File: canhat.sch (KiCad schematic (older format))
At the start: 24 parts, among them J1 Raspberry_Pi_2_3, J2 CAN In, J3 CAN Out, U1 MCP2515-xSO, U2 SN65HVD234, U3 AT24C32-SSHM, Y1 16MHz

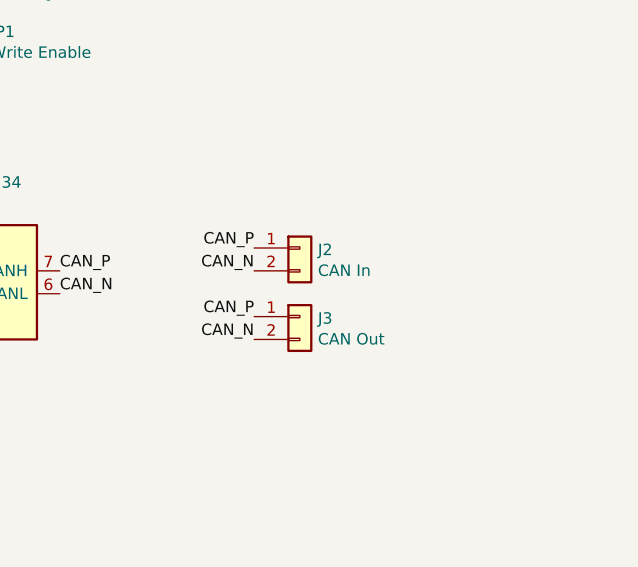
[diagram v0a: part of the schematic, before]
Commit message: Replaced CAN terminals with single block
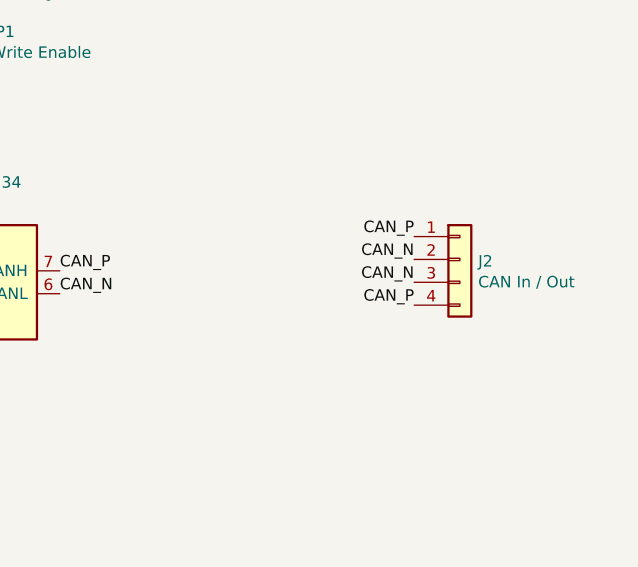
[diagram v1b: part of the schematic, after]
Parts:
- removed J2: CAN In, TerminalBlock_TE-Connectivity:TerminalBlock_TE_282834-2_1x02_P2.54mm_Horizontal, symbol Connector_Generic:Conn_01x02
- removed J3: CAN Out, TerminalBlock_TE-Connectivity:TerminalBlock_TE_282834-2_1x02_P2.54mm_Horizontal, symbol Connector_Generic:Conn_01x02
- added J2: CAN In / Out, TerminalBlock_TE-Connectivity:TerminalBlock_TE_282834-4_1x04_P2.54mm_Horizontal, symbol Connector_Generic:Conn_01x04
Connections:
- net CAN_N: now also J2.2 (Pin_2), J2.3 (Pin_3)
- net CAN_P: now also J2.1 (Pin_1), J2.4 (Pin_4)
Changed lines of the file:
@@
 Sheet 1 1
 Title "CAN HAT for Raspberry Pi"
-Date "2019-04-05"
-Rev "1"
+Date "2019-04-29"
+Rev "2"
 Comp "© 2019 Gregor Riepl"
 Comment1 ""
@@
 $EndComp
 $Comp
-L Connector_Generic:Conn_01x02 J2
-U 1 1 5CA2AC48
-P 9450 3200
-F 0 "J2" H 9529 3192 50  0000 L CNN
-F 1 "CAN In" H 9529 3101 50  0000 L CNN
-F 2 "TerminalBlock_TE-Connectivity:TerminalBlock_TE_282834-2_1x02_P2.54mm_Horizontal" H 9450 3200 50  0001 C CNN
-F 3 "~" H 9450 3200 50  0001 C CNN
-	1    9450 3200
-	1    0    0    -1
-$EndComp
-$Comp
-L Connector_Generic:Conn_01x02 J3
-U 1 1 5CA2B324
-P 9450 3500
-F 0 "J3" H 9529 3492 50  0000 L CNN
-F 1 "CAN Out" H 9529 3401 50  0000 L CNN
-F 2 "TerminalBlock_TE-Connectivity:TerminalBlock_TE_282834-2_1x02_P2.54mm_Horizontal" H 9450 3500 50  0001 C CNN
-F 3 "~" H 9450 3500 50  0001 C CNN
-	1    9450 3500
-	1    0    0    -1
-$EndComp
-$Comp
 L Mechanical:MountingHole H1
 U 1 1 5CA2E828
@@
 Text Label 8400 3400 0    50   ~ 0
 CAN_N
-Text Label 9250 3200 2    50   ~ 0
+Text Label 9950 3150 2    50   ~ 0
 CAN_P
-Text Label 9250 3500 2    50   ~ 0
+Text Label 9950 3450 2    50   ~ 0
 CAN_P
-Text Label 9250 3300 2    50   ~ 0
+Text Label 9950 3250 2    50   ~ 0
 CAN_N
-Text Label 9250 3600 2    50   ~ 0
+Text Label 9950 3350 2    50   ~ 0
 CAN_N
 $Comp
@@
 	1    0    0    -1
 $EndComp
+$Comp
+L Connector_Generic:Conn_01x04 J2
+U 1 1 5CC6B3E9
+P 10150 3250
+F 0 "J2" H 10230 3242 50  0000 L CNN
+F 1 "CAN In / Out" H 10230 3151 50  0000 L CNN
+F 2 "TerminalBlock_TE-Connectivity:TerminalBlock_TE_282834-4_1x04_P2.54mm_Horizontal" H 10150 3250 50  0001 C CNN
+F 3 "~" H 10150 3250 50  0001 C CNN
+	1    10150 3250
+	1    0    0    -1
+$EndComp

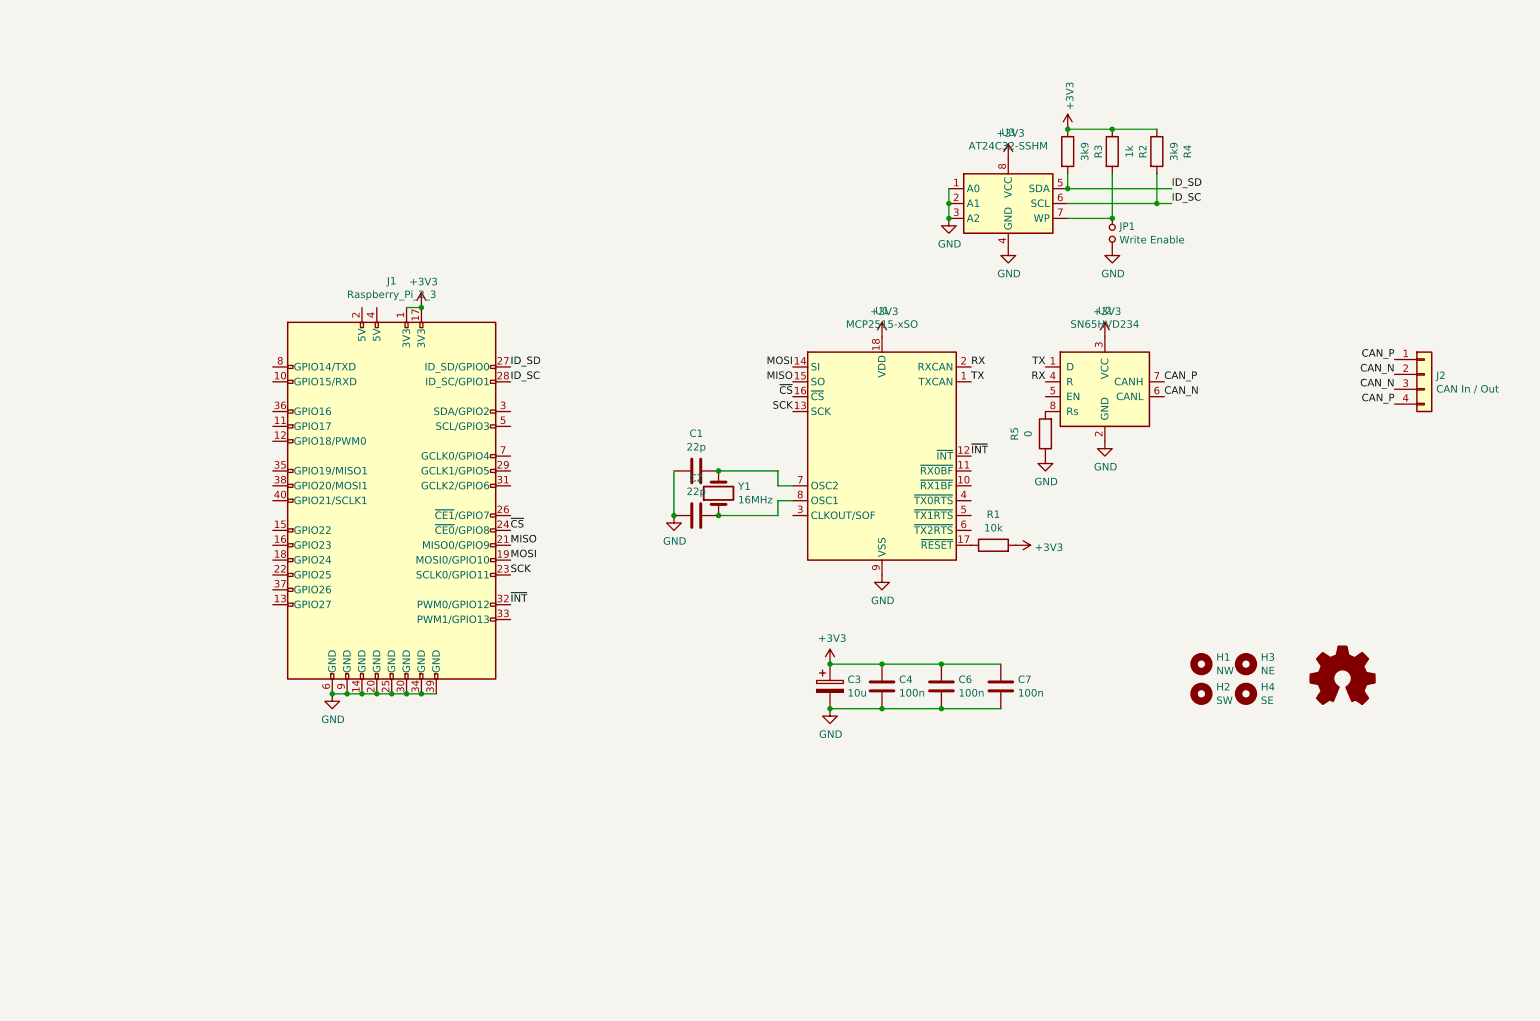
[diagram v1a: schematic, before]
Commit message: Added 5V power terminal
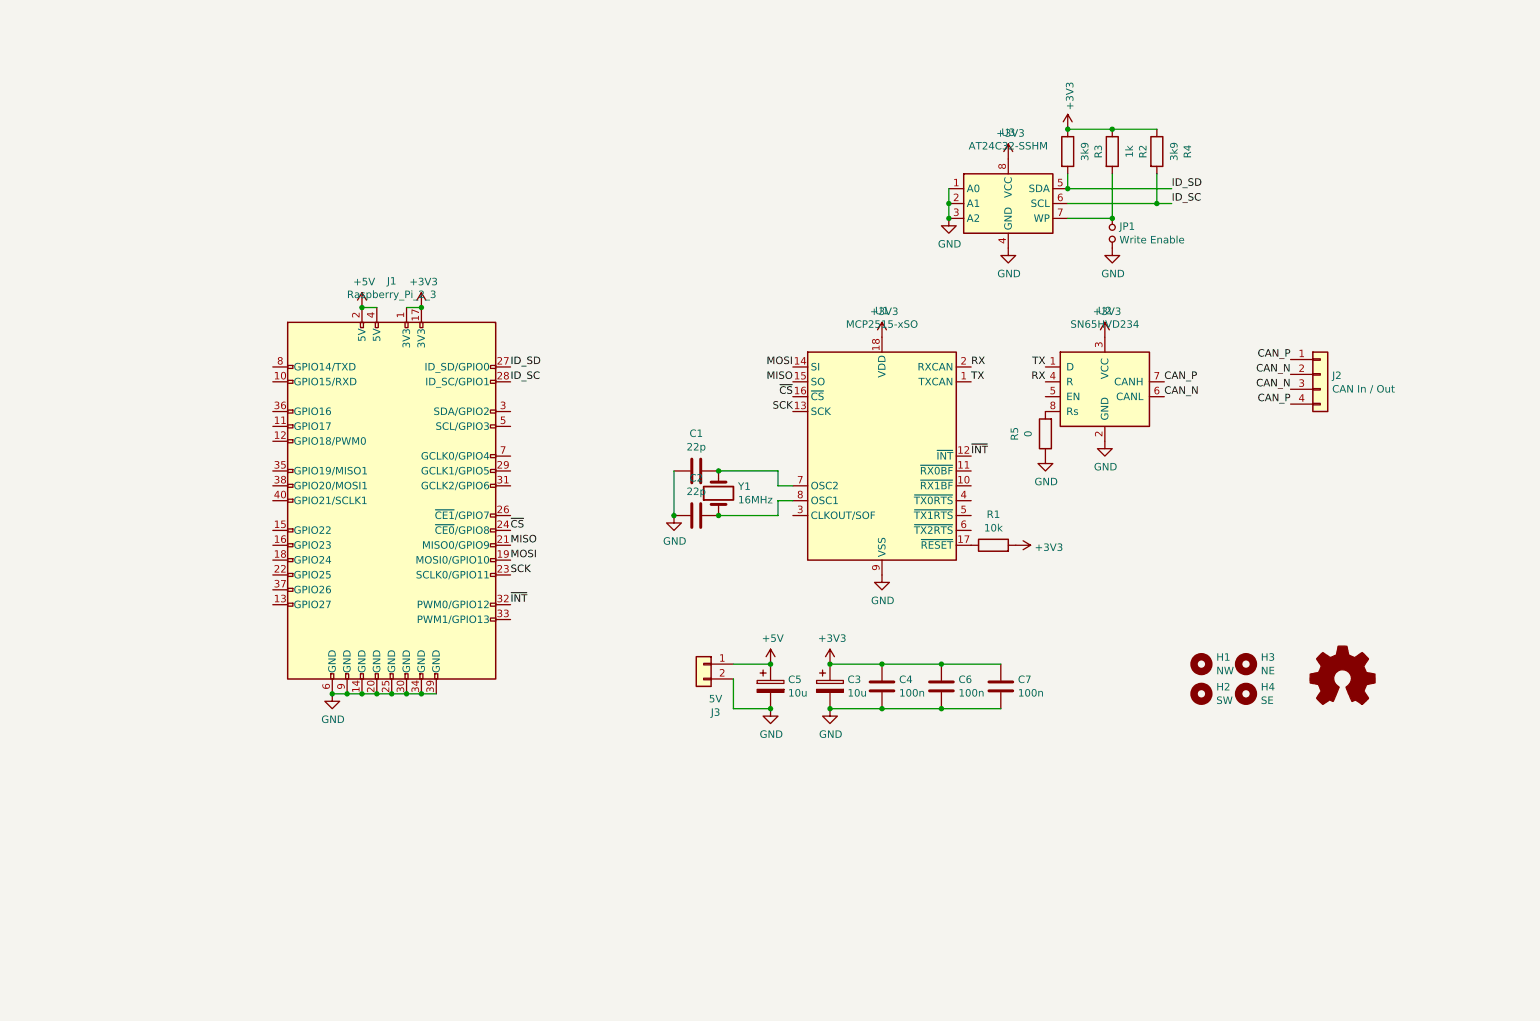
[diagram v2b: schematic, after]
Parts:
- added C5: 10u, Capacitor_Tantalum_SMD:CP_EIA-7343-31_Kemet-D_Pad2.25x2.55mm_HandSolder, symbol Device:CP
- added J3: 5V, TerminalBlock_TE-Connectivity:TerminalBlock_TE_282834-2_1x02_P2.54mm_Horizontal, symbol Connector_Generic:Conn_01x02
- C3: footprint Capacitor_THT:CP_Radial_D5.0mm_P2.00mm -> Capacitor_Tantalum_SMD:CP_EIA-7343-31_Kemet-D_Pad2.25x2.55mm_HandSolder
- Y1: footprint Crystal:Crystal_SMD_HC49-SD_HandSoldering -> Crystal:Crystal_SMD_HC49-SD
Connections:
- net GND: now also C5.2, J3.2 (Pin_2)
- net +5V: now reaches J1.2 (5V)
- net +5V: now also J1.4 (5V), C5.1, J3.1 (Pin_1)
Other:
- moved on the sheet: J2
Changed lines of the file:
@@
 Sheet 1 1
 Title "CAN HAT for Raspberry Pi"
-Date "2019-04-29"
+Date "2019-05-01"
 Rev "2"
 Comp "© 2019 Gregor Riepl"
@@
 F 0 "Y1" V 5446 3919 50  0000 R CNN
 F 1 "16MHz" V 5355 3919 50  0000 R CNN
-F 2 "Crystal:Crystal_SMD_HC49-SD_HandSoldering" H 5400 4050 50  0001 C CNN
+F 2 "Crystal:Crystal_SMD_HC49-SD" H 5400 4050 50  0001 C CNN
 F 3 "~" H 5400 4050 50  0001 C CNN
 	1    5400 4050
@@
 F 0 "C3" H 6268 5396 50  0000 L CNN
 F 1 "10u" H 6268 5305 50  0000 L CNN
-F 2 "Capacitor_THT:CP_Radial_D5.0mm_P2.00mm" H 6188 5200 50  0001 C CNN
+F 2 "Capacitor_Tantalum_SMD:CP_EIA-7343-31_Kemet-D_Pad2.25x2.55mm_HandSolder" H 6188 5200 50  0001 C CNN
 F 3 "~" H 6150 5350 50  0001 C CNN
 	1    6150 5350
@@
 Text Label 8400 3400 0    50   ~ 0
 CAN_N
-Text Label 9950 3150 2    50   ~ 0
+Text Label 9250 3150 2    50   ~ 0
 CAN_P
-Text Label 9950 3450 2    50   ~ 0
+Text Label 9250 3450 2    50   ~ 0
 CAN_P
-Text Label 9950 3250 2    50   ~ 0
+Text Label 9250 3250 2    50   ~ 0
 CAN_N
-Text Label 9950 3350 2    50   ~ 0
+Text Label 9250 3350 2    50   ~ 0
 CAN_N
 $Comp
@@
 L Connector_Generic:Conn_01x04 J2
 U 1 1 5CC6B3E9
-P 10150 3250
-F 0 "J2" H 10230 3242 50  0000 L CNN
-F 1 "CAN In / Out" H 10230 3151 50  0000 L CNN
-F 2 "TerminalBlock_TE-Connectivity:TerminalBlock_TE_282834-4_1x04_P2.54mm_Horizontal" H 10150 3250 50  0001 C CNN
-F 3 "~" H 10150 3250 50  0001 C CNN
-	1    10150 3250
-	1    0    0    -1
-$EndComp
+P 9450 3250
+F 0 "J2" H 9530 3242 50  0000 L CNN
+F 1 "CAN In / Out" H 9530 3151 50  0000 L CNN
+F 2 "TerminalBlock_TE-Connectivity:TerminalBlock_TE_282834-4_1x04_P2.54mm_Horizontal" H 9450 3250 50  0001 C CNN
+F 3 "~" H 9450 3250 50  0001 C CNN
+	1    9450 3250
+	1    0    0    -1
+$EndComp
+$Comp
+L Connector_Generic:Conn_01x02 J3
+U 1 1 5CC8D2CE
+P 5300 5200
+F 0 "J3" H 5220 4875 50  0000 C CNN
+F 1 "5V" H 5220 4966 50  0000 C CNN
+F 2 "TerminalBlock_TE-Connectivity:TerminalBlock_TE_282834-2_1x02_P2.54mm_Horizontal" H 5300 5200 50  0001 C CNN
+F 3 "~" H 5300 5200 50  0001 C CNN
+	1    5300 5200
+	-1   0    0    -1
+$EndComp
+$Comp
+L power:+5V #PWR0111
+U 1 1 5CC8D443
+P 3000 2800
+F 0 "#PWR0111" H 3000 2650 50  0001 C CNN
+F 1 "+5V" H 3015 2973 50  0000 C CNN
+F 2 "" H 3000 2800 50  0001 C CNN
+F 3 "" H 3000 2800 50  0001 C CNN
+	1    3000 2800
+	1    0    0    -1
+$EndComp
+Wire Wire Line
+	3100 2800 3000 2800
+Connection ~ 3000 2800
+$Comp
+L power:+5V #PWR0112
+U 1 1 5CC8D96C
+P 5750 5200
+F 0 "#PWR0112" H 5750 5050 50  0001 C CNN
+F 1 "+5V" H 5765 5373 50  0000 C CNN
+F 2 "" H 5750 5200 50  0001 C CNN
+F 3 "" H 5750 5200 50  0001 C CNN
+	1    5750 5200
+	1    0    0    -1
+$EndComp
+$Comp
+L Device:CP C5
+U 1 1 5CC8DA64
+P 5750 5350
+F 0 "C5" H 5868 5396 50  0000 L CNN
+F 1 "10u" H 5868 5305 50  0000 L CNN
+F 2 "Capacitor_Tantalum_SMD:CP_EIA-7343-31_Kemet-D_Pad2.25x2.55mm_HandSolder" H 5788 5200 50  0001 C CNN
+F 3 "~" H 5750 5350 50  0001 C CNN
+	1    5750 5350
+	1    0    0    -1
+$EndComp
+$Comp
+L power:GND #PWR0114
+U 1 1 5CC8DAAA
+P 5750 5500
+F 0 "#PWR0114" H 5750 5250 50  0001 C CNN
+F 1 "GND" H 5755 5327 50  0000 C CNN
+F 2 "" H 5750 5500 50  0001 C CNN
+F 3 "" H 5750 5500 50  0001 C CNN
+	1    5750 5500
+	1    0    0    -1
+$EndComp
+Wire Wire Line
+	5500 5200 5750 5200
+Connection ~ 5750 5200
+Wire Wire Line
+	5500 5500 5750 5500
+Connection ~ 5750 5500
+Wire Wire Line
+	5500 5300 5500 5500
 $EndSCHEMATC

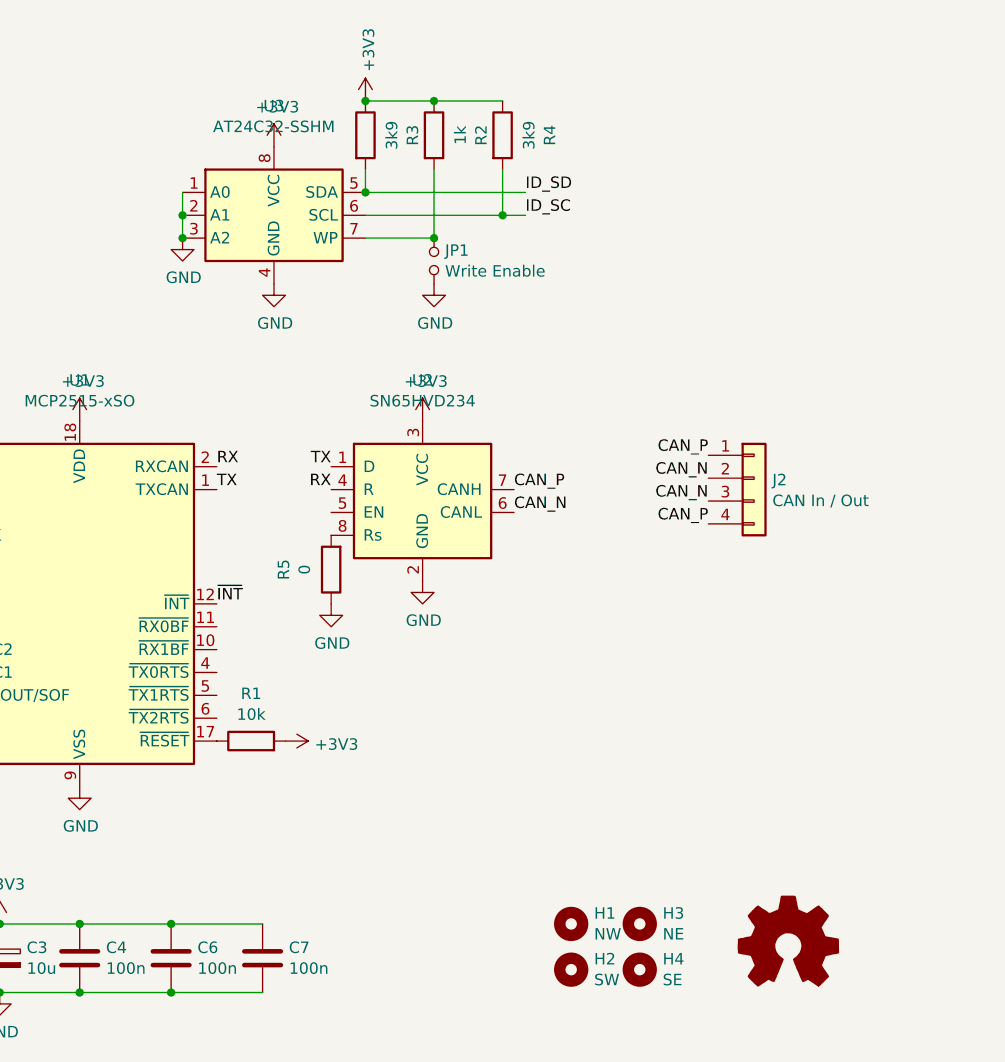
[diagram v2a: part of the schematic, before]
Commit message: Split off power plane for transceiver for 3.3/5V power
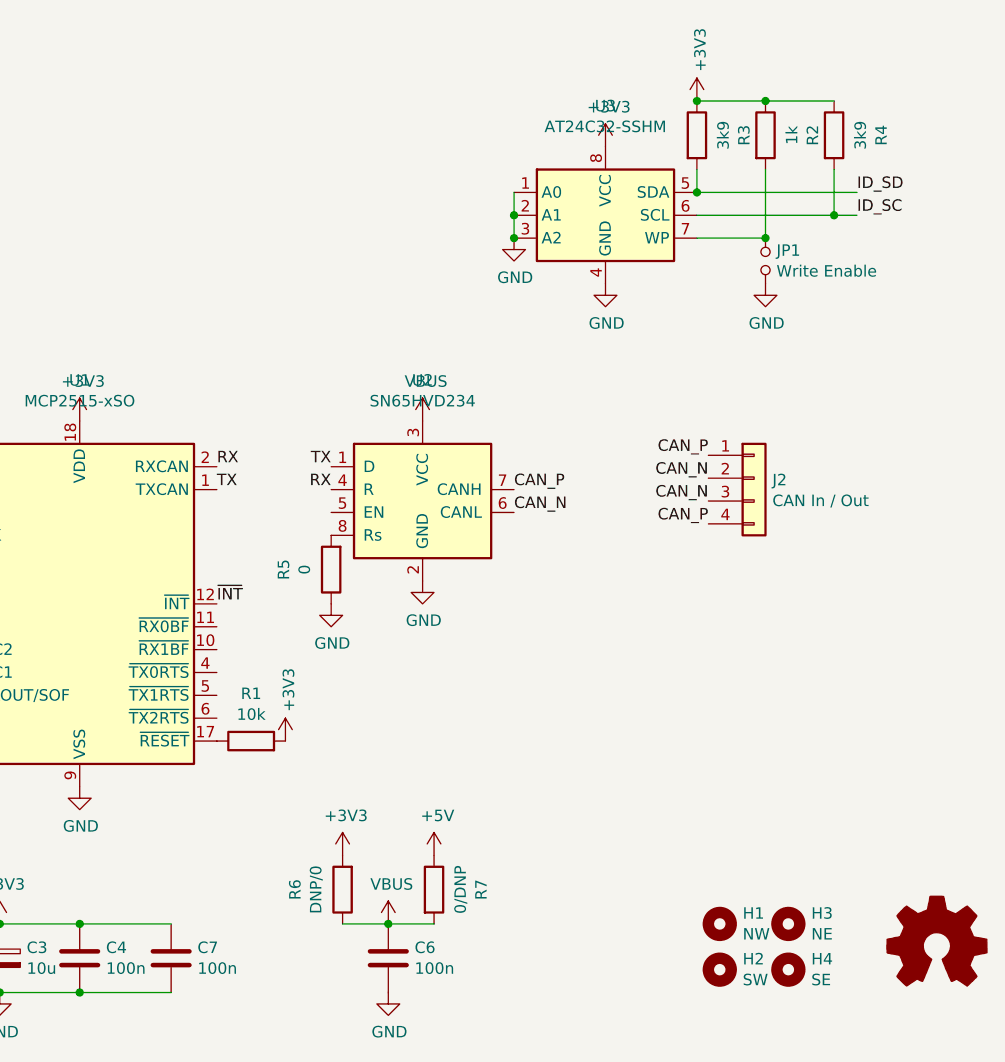
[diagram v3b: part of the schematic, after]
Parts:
- added R6: DNP/0, Resistor_SMD:R_0805_2012Metric_Pad1.15x1.40mm_HandSolder, symbol Device:R
- added R7: 0/DNP, Resistor_SMD:R_0805_2012Metric_Pad1.15x1.40mm_HandSolder, symbol Device:R
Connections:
- net +3V3: now also R6.2; no longer C6.1, U2.3 (VCC)
- net +5V: now also R7.1
- new net VBUS: C6.1, R6.1, R7.2, U2.3 (VCC)
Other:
- moved on the sheet: C6, C7, H1, H2, H3, H4, JP1, R2, R3, R4, U3

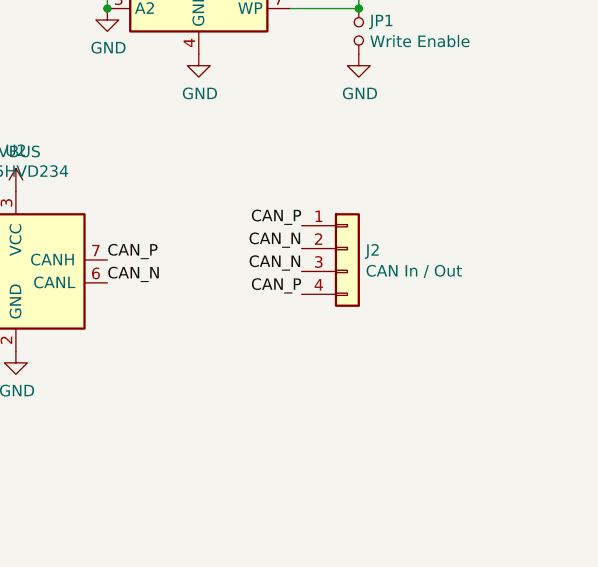
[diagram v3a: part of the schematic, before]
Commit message: Redid layout to shorten long traces
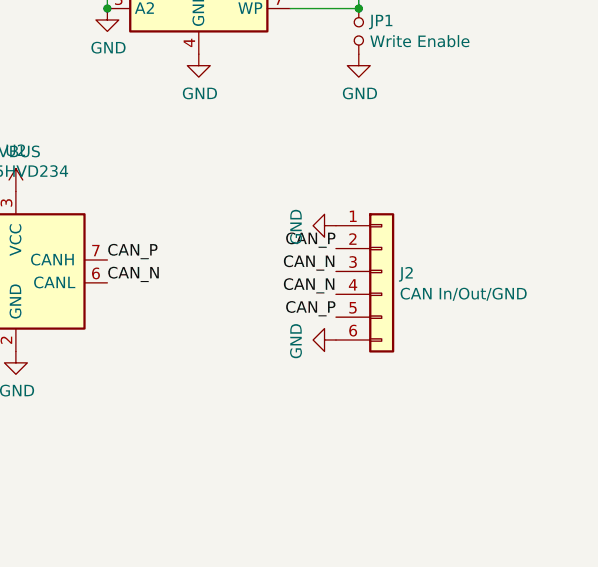
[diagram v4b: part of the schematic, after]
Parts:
- removed J2: CAN In / Out, TerminalBlock_TE-Connectivity:TerminalBlock_TE_282834-4_1x04_P2.54mm_Horizontal, symbol Connector_Generic:Conn_01x04
- added J2: CAN In/Out/GND, TerminalBlock_TE-Connectivity:TerminalBlock_TE_282834-6_1x06_P2.54mm_Horizontal, symbol Connector_Generic:Conn_01x06
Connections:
- net CAN_N: now also J2.3 (Pin_3), J2.4 (Pin_4)
- net CAN_P: now also J2.2 (Pin_2), J2.5 (Pin_5)
- net GND: now also J2.1 (Pin_1), J2.6 (Pin_6)
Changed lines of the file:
@@
 Sheet 1 1
 Title "CAN HAT for Raspberry Pi"
-Date "2019-05-01"
-Rev "2"
+Date "2019-05-15"
+Rev "3"
 Comp "© 2019 Gregor Riepl"
 Comment1 ""
@@
 Text Label 8400 3400 0    50   ~ 0
 CAN_N
-Text Label 9250 3150 2    50   ~ 0
+Text Label 9400 3250 2    50   ~ 0
 CAN_P
-Text Label 9250 3450 2    50   ~ 0
+Text Label 9400 3550 2    50   ~ 0
 CAN_P
-Text Label 9250 3250 2    50   ~ 0
+Text Label 9400 3350 2    50   ~ 0
 CAN_N
-Text Label 9250 3350 2    50   ~ 0
+Text Label 9400 3450 2    50   ~ 0
 CAN_N
 $Comp
@@
 $EndComp
 $Comp
-L Connector_Generic:Conn_01x04 J2
-U 1 1 5CC6B3E9
-P 9450 3250
-F 0 "J2" H 9530 3242 50  0000 L CNN
-F 1 "CAN In / Out" H 9530 3151 50  0000 L CNN
-F 2 "TerminalBlock_TE-Connectivity:TerminalBlock_TE_282834-4_1x04_P2.54mm_Horizontal" H 9450 3250 50  0001 C CNN
-F 3 "~" H 9450 3250 50  0001 C CNN
-	1    9450 3250
-	1    0    0    -1
-$EndComp
-$Comp
 L Connector_Generic:Conn_01x02 J3
 U 1 1 5CC8D2CE
@@
 	1    0    0    -1
 $EndComp
+$Comp
+L Connector_Generic:Conn_01x06 J2
+U 1 1 5CDB0786
+P 9600 3350
+F 0 "J2" H 9679 3342 50  0000 L CNN
+F 1 "CAN In/Out/GND" H 9679 3251 50  0000 L CNN
+F 2 "TerminalBlock_TE-Connectivity:TerminalBlock_TE_282834-6_1x06_P2.54mm_Horizontal" H 9600 3350 50  0001 C CNN
+F 3 "~" H 9600 3350 50  0001 C CNN
+	1    9600 3350
+	1    0    0    -1
+$EndComp
+$Comp
+L power:GND #PWR0119
+U 1 1 5CDB15C9
+P 9400 3650
+F 0 "#PWR0119" H 9400 3400 50  0001 C CNN
+F 1 "GND" H 9405 3477 50  0000 C CNN
+F 2 "" H 9400 3650 50  0001 C CNN
+F 3 "" H 9400 3650 50  0001 C CNN
+	1    9400 3650
+	0    1    1    0
+$EndComp
+$Comp
+L power:GND #PWR0120
+U 1 1 5CDB1625
+P 9400 3150
+F 0 "#PWR0120" H 9400 2900 50  0001 C CNN
+F 1 "GND" H 9405 2977 50  0000 C CNN
+F 2 "" H 9400 3150 50  0001 C CNN
+F 3 "" H 9400 3150 50  0001 C CNN
+	1    9400 3150
+	0    1    1    0
+$EndComp
 $EndSCHEMATC
